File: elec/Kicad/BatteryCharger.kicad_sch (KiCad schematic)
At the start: 7 parts, among them J2 B2B-XH-A, U3 MCP73831

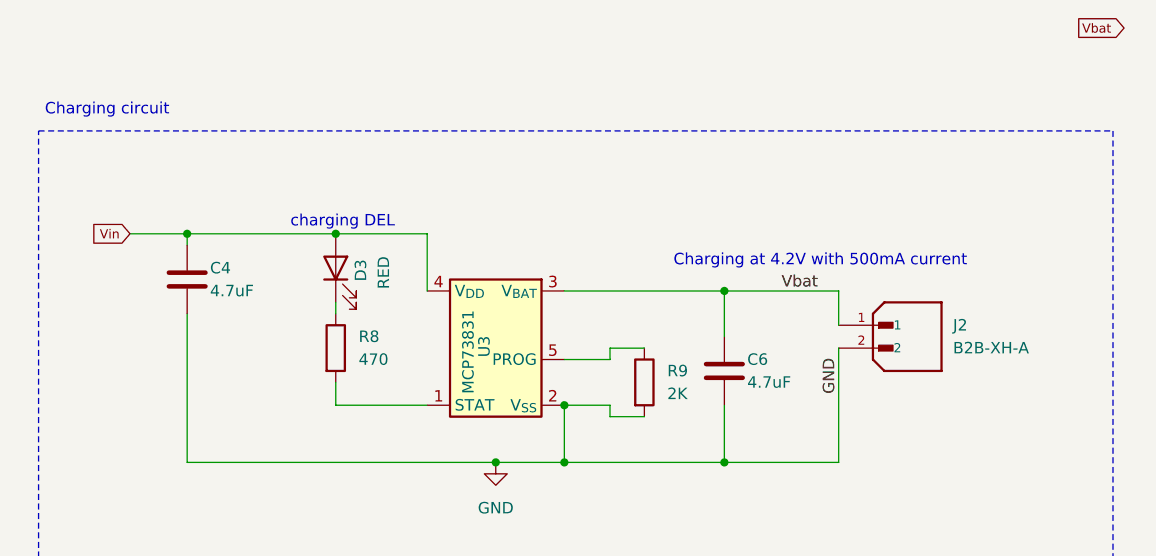
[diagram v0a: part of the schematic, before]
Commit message: Presque finin la la gestion de la batterie (faire les dels demains)
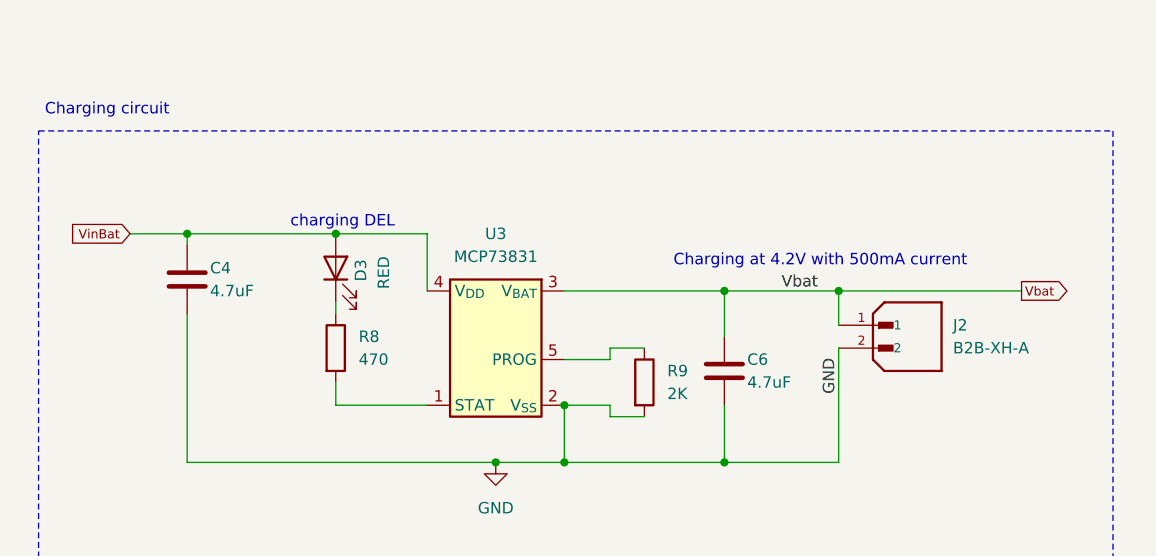
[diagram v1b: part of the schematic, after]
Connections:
- net Vin renamed VinBat
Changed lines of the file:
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@@
 		(color 0 0 0 0)
 	)
+	(junction
+		(at 137.16 60.96)
+		(diameter 0)
+		(color 0 0 0 0)
+	)
 	(wire
 		(pts
@@
 		(pts
 			(xy 81.28 71.12) (xy 81.28 73.66)
+		)
+		(stroke
+			(width 0)
+			(type default)
+		)
+	)
+	(wire
+		(pts
+			(xy 137.16 60.96) (xy 157.48 60.96)
 		)
 		(stroke
@@
 	(global_label "Vbat"
 		(shape output)
-		(at 163.83 31.75 0)
+		(at 157.48 60.96 0)
 		(fields_autoplaced yes)
 		(effects
@@
 		)
 		(property "Intersheetrefs" "${INTERSHEET_REFS}"
-			(at 169.5078 31.75 0)
+			(at 163.1578 60.96 0)
 			(effects
 				(font
@@
 		)
 	)
-	(global_label "Vin"
+	(global_label "VinBat"
 		(shape input)
 		(at 58.42 54.61 180)
@@
 		)
 		(property "Intersheetrefs" "${INTERSHEET_REFS}"
-			(at 53.7582 54.61 0)
+			(at 51.2424 54.61 0)
 			(effects
 				(font
@@
 		(fields_autoplaced yes)
 		(property "Reference" "U3"
-			(at 97.79 68.326 90)
+			(at 99.06 54.61 0)
 			(effects
 				(font
 					(size 1.27 1.27)
 				)
-				(justify left)
 			)
 		)
 		(property "Value" "MCP73831"
-			(at 96.012 72.39 90)
+			(at 99.06 57.15 0)
 			(effects
 				(font
 					(size 1.27 1.27)
 				)
-				(justify left)
-			)
-		)
+			)
+		)

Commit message: sa progresse. Battery management fini + humidity/temp sensor + bouton
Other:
- note added: "LED qui indique que la battery recharge"
- note removed: "charging DEL"
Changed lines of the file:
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@@
 		)
 	)
-	(text "charging DEL\n"
+	(text "LED qui indique que la battery recharge"
 		(exclude_from_sim no)
 		(at 82.042 53.34 0)

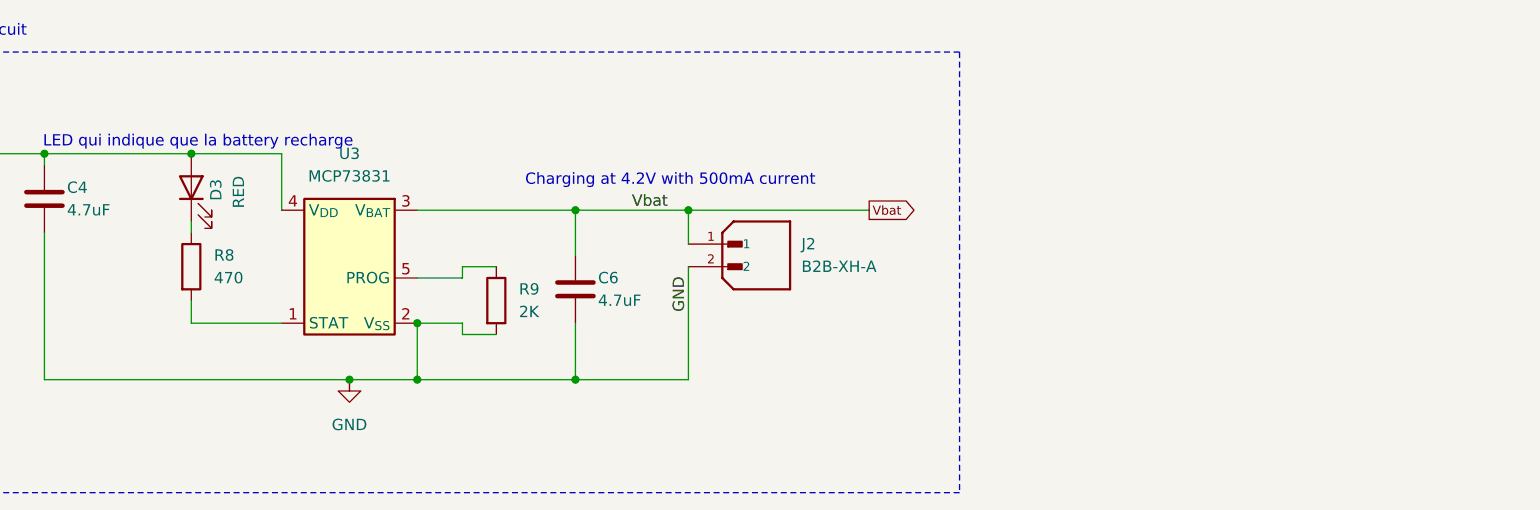
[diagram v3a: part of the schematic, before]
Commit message: add a few footprint
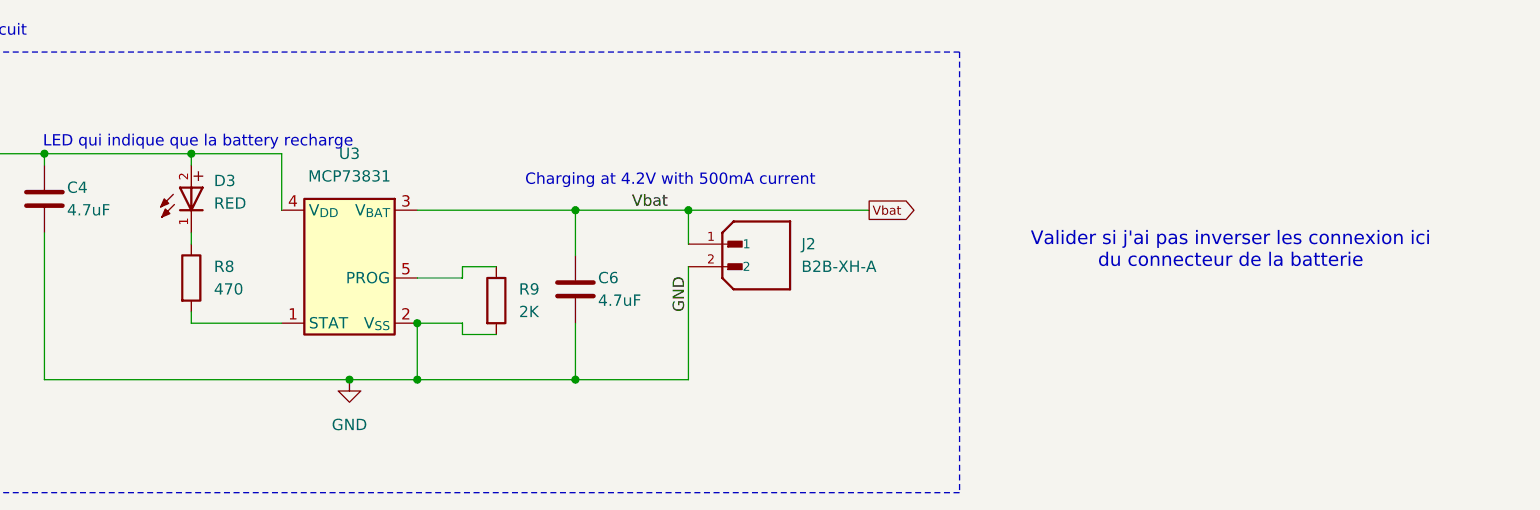
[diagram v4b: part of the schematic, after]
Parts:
- removed D3: RED, symbol Device:LED
- added D3: RED, SMD_LED_0603:WL-SMCD_0603, symbol WL-SMCD_0603:WL-SMCD_0603
- C4, C6: footprint (none) -> Capacitor_SMD:C_0603_1608Metric_Pad1.08x0.95mm_HandSolder
- R8, R9: footprint (none) -> Resistor_SMD:R_0603_1608Metric_Pad0.98x0.95mm_HandSolder
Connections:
- net VinBat: now also D3.2
- net at R8.1: now also D3.1
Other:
- note added: "Valider si j'ai pas inverser les connexion ici du connecteur de la batterie"
- moved on the sheet: R8

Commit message: J'ai ajouter des power Flag pour spécifier a Kicad que c'est chill (faut qu'il apprenne a ce géré quand même)
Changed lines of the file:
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@@
+		(color 0 0 0 0)
+	)
+	(junction
+		(at 91.44 54.61)
+		(diameter 0)
 		(color 0 0 0 0)
 	)
@@
 	(text "LED qui indique que la battery recharge"
 		(exclude_from_sim no)
-		(at 82.042 53.34 0)
+		(at 70.104 47.244 0)
 		(effects
 			(font
@@
 			)
 		)
+	)
+	(symbol
+		(lib_id "power:PWR_FLAG")
+		(at 91.44 54.61 0)
+		(unit 1)
+		(exclude_from_sim no)
+		(in_bom yes)
+		(on_board yes)
+		(dnp no)
+		(fields_autoplaced yes)
+		(property "Reference" "#FLG04"
+			(at 91.44 52.705 0)
+			(effects
+				(font
+					(size 1.27 1.27)
+				)
+				(hide yes)
+			)
+		)
+		(property "Value" "PWR_FLAG"
+			(at 91.44 49.53 0)
+			(effects
+				(font
+					(size 1.27 1.27)
+				)
+			)
+		)
+		(property "Footprint" ""
+			(at 91.44 54.61 0)
+			(effects
+				(font
+					(size 1.27 1.27)
+				)
+				(hide yes)
+			)
+		)
+		(property "Datasheet" "~"
+			(at 91.44 54.61 0)
+			(effects
+				(font
+					(size 1.27 1.27)
+				)
+				(hide yes)
+			)
+		)
+		(property "Description" "Special symbol for telling ERC where power comes from"
+			(at 91.44 54.61 0)
+			(effects
+				(font
+					(size 1.27 1.27)
+				)
+				(hide yes)
+			)
+		)
+		(pin "1"
+		)
+		(instances
+			(project ""
+				(path "/a1545928-1195-40b9-b3c4-78f837012afb/47f0fc71-ff78-496f-bb04-036a9aeaa71c/6f59428e-8e72-4854-8d86-784df1ffb46d/486d1226-8ba5-4168-8f64-8ace2267ed6c"
+					(reference "#FLG04")
+					(unit 1)
+				)
+			)
+		)

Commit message: commencer le PCB vite fait
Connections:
- net GND: now also J2.1; no longer J2.2
- net Vbat: now also J2.2; no longer J2.1
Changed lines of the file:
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@@
+	)
+	(symbol
+		(lib_id "B2B-XH-A:B2B-XH-A")
+		(at 144.78 64.77 0)
+		(mirror x)
+		(unit 1)
+		(exclude_from_sim no)
+		(in_bom yes)
+		(on_board yes)
+		(dnp no)
+		(property "Reference" "J2"
+			(at 149.86 67.3101 0)
+			(effects
+				(font
+					(size 1.27 1.27)
+				)
+				(justify left)
+			)
+		)
+		(property "Value" "B2B-XH-A"
+			(at 149.86 64.7701 0)
+			(effects
+				(font
+					(size 1.27 1.27)
+				)
+				(justify left)
+			)
+		)
+		(property "Footprint" "Connector_JST:JST_XH_B2B-XH-AM_1x02_P2.50mm_Vertical"
+			(at 144.78 64.77 0)
+			(effects
+				(font
+					(size 1.27 1.27)
+				)
+				(justify bottom)
+				(hide yes)
+			)
+		)
+		(property "Datasheet" ""
+			(at 144.78 64.77 0)
+			(effects
+				(font
+					(size 1.27 1.27)
+				)
+				(hide yes)
+			)
+		)
+		(property "Description" ""
+			(at 144.78 64.77 0)
+			(effects
+				(font
+					(size 1.27 1.27)
+				)
+				(hide yes)
+			)
+		)
+		(property "PARTREV" "N/A"
+			(at 144.78 64.77 0)
+			(effects
+				(font
+					(size 1.27 1.27)
+				)
+				(justify bottom)
+				(hide yes)
+			)
+		)
+		(property "STANDARD" "Manufacturer Recommendations"
+			(at 144.78 64.77 0)
+			(effects
+				(font
+					(size 1.27 1.27)
+				)
+				(justify bottom)
+				(hide yes)
+			)
+		)
+		(property "MAXIMUM_PACKAGE_HEIGHT" "7 mm"
+			(at 144.78 64.77 0)
+			(effects
+				(font
+					(size 1.27 1.27)
+				)
+				(justify bottom)
+				(hide yes)
+			)
+		)
+		(property "MANUFACTURER" "JST Sales America Inc."
+			(at 144.78 64.77 0)
+			(effects
+				(font
+					(size 1.27 1.27)
+				)
+				(justify bottom)
+				(hide yes)
+			)
+		)
+		(pin "1"
+		)
+		(pin "2"
+		)
+		(instances
+			(project "rulerSchematic"
+				(path "/a1545928-1195-40b9-b3c4-78f837012afb/47f0fc71-ff78-496f-bb04-036a9aeaa71c/6f59428e-8e72-4854-8d86-784df1ffb46d/486d1226-8ba5-4168-8f64-8ace2267ed6c"
+					(reference "J2")
+					(unit 1)
+				)
+			)
+		)
 	)
 	(symbol
@@
 					(unit 1)
 				)
-			)
-		)
-	)
-	(symbol
-		(lib_id "B2B-XH-A:B2B-XH-A")
-		(at 144.78 67.31 0)
-		(unit 1)
-		(exclude_from_sim no)
-		(in_bom yes)
-		(on_board yes)
-		(dnp no)
-		(fields_autoplaced yes)
-		(property "Reference" "J2"
-			(at 149.86 64.7699 0)
-			(effects
-				(font
-					(size 1.27 1.27)
-				)
-				(justify left)
-			)
-		)
-		(property "Value" "B2B-XH-A"
-			(at 149.86 67.3099 0)
-			(effects
-				(font
-					(size 1.27 1.27)
-				)
-				(justify left)
-			)
-		)
-		(property "Footprint" "Connector_JST:JST_XH_B2B-XH-AM_1x02_P2.50mm_Vertical"
-			(at 144.78 67.31 0)
-			(effects
-				(font
-					(size 1.27 1.27)
-				)
-				(justify bottom)
-				(hide yes)
-			)
-		)
-		(property "Datasheet" ""
-			(at 144.78 67.31 0)
-			(effects
-				(font
-					(size 1.27 1.27)
-				)
-				(hide yes)
-			)
-		)
-		(property "Description" ""
-			(at 144.78 67.31 0)
-			(effects
-				(font
-					(size 1.27 1.27)
-				)
-				(hide yes)
-			)
-		)
-		(property "PARTREV" "N/A"
-			(at 144.78 67.31 0)
-			(effects
-				(font
-					(size 1.27 1.27)
-				)
-				(justify bottom)
-				(hide yes)
-			)
-		)
-		(property "STANDARD" "Manufacturer Recommendations"
-			(at 144.78 67.31 0)
-			(effects
-				(font
-					(size 1.27 1.27)
-				)
-				(justify bottom)
-				(hide yes)
-			)
-		)
-		(property "MAXIMUM_PACKAGE_HEIGHT" "7 mm"
-			(at 144.78 67.31 0)
-			(effects
-				(font
-					(size 1.27 1.27)
-				)
-				(justify bottom)
-				(hide yes)
-			)
-		)
-		(property "MANUFACTURER" "JST Sales America Inc."
-			(at 144.78 67.31 0)
-			(effects
-				(font
-					(size 1.27 1.27)
-				)
-				(justify bottom)
-				(hide yes)
-			)
-		)
-		(pin "1"
-		)
-		(pin "2"
-		)
-		(instances
-			(project "rulerSchematic"
-				(path "/a1545928-1195-40b9-b3c4-78f837012afb/47f0fc71-ff78-496f-bb04-036a9aeaa71c/6f59428e-8e72-4854-8d86-784df1ffb46d/486d1226-8ba5-4168-8f64-8ace2267ed6c"
-					(reference "J2")
-					(unit 1)
-				)

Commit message: igfukhj.hlk
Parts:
- added H1, H2, H3, H4: MountingHole, MountingHole:MountingHole_2.2mm_M2, symbol Mechanical:MountingHole
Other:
- note added: "M2 Screw"
- note added: "Mounting Hole Battery + LCD"
